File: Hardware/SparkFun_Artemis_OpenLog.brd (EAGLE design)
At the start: 30.5 x 30.5 mm, 140 parts, among them J14 CORTEX_JTAG, J6 MICRO-SD, Q1 20V/0.2A/8MHz/1.2Ω/1Vth, Q10 20V/0.2A/8MHz/1.2Ω/1Vth, Q2 20V/4.2A/52mΩ/1.4W, Q3 20V/0.2A/8MHz/1.2Ω/1Vth, Q7 20V/0.2A/8MHz/1.2Ω/1Vth, Q9 20V/0.2A/8MHz/1.2Ω/1Vth, U1 3.0V Supervisor, U10 CH340E, U13 9DoF IMU, U14 1.8V/100mA, U2 MCP73831, U3 3.3V, U4 3.3V, U8 ARTEMIS_MODULE, Y3 32.768kHz

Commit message: Attempts to update just the Eagle design
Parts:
- removed C51, C52: 0.1uF, SparkFun-Capacitors:0402-TIGHT
- removed C53, C54: 1.0uF, SparkFun-Capacitors:0402-TIGHT
- removed Q1, Q10, Q3, Q7, Q9: 20V/0.2A/8MHz/1.2Ω/1Vth, SparkFun-DiscreteSemi:SOT-416FL
- removed R40, R41, R44, R45, R46, R47, R48: 2.2k, SparkFun-Resistors:0402-TIGHT
- removed R49: DNP, SparkFun-Resistors:0402-TIGHT
- removed U13: 9DoF IMU, SparkFun-Sensors:QFN24-3X3-ICM-20948
- removed U14: 1.8V/100mA, SparkFun-IC-Power:SC70
- added C10, C11, C9: 0.1uF, SparkFun-Capacitors:0402
- added C6, C8: 22pF, SparkFun-Capacitors:0402-TIGHT
- added R10, R11: 4.7k, SparkFun-Resistors:0402-TIGHT
- added R12, R9: 100k, SparkFun-Resistors:0402-TIGHT
- added U5: BNO086, bno086:LGA-28
- added Y1: 32.768kHz, SparkFun-Clocks:CRYSTAL-SMD-3.2X1.5MM
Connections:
- removed net ICM-20948-LV_!CS!: Q9.2, R46.1, U13.22
- removed net ICM-20948-LV_#_1.8V: C52.1, C53.1, Q1.1, Q10.1, Q3.1, Q7.1, Q9.1, R40.2, R41.2, R44.2, R46.2, R48.2, U13.13, U13.8, U14.5
- removed net ICM-20948-LV_INT: Q7.2, R44.1, U13.12
- removed net ICM-20948-LV_SCK: Q1.2, R40.1, U13.23
- removed net ICM-20948-LV_SDI: Q3.2, R41.1, U13.24
- removed net ICM-20948-LV_SDO: Q10.2, R48.1, U13.9
- removed net N$30: C51.1, U13.10
- new net !RST: R9.1, U5.11
- new net N$2: C8.1, U5.27, Y1.P$2
- new net N$3: C6.1, U5.26, Y1.P$1
- new net N$4: C9.1, U5.9
- new net N$5: R12.1, U5.4
- new net S_SCL: R11.1, U5.15
- new net S_SDA: R10.1, U5.16
- net 3.3V: now also C10.1, C11.1, R10.2, R11.2, R12.2, R9.2, U5.28, U5.3, U5.5, U5.6; no longer C54.1, R45.2, R47.2, R49.2, U14.1
- net GND: now also C10.2, C11.2, C6.2, C8.2, C9.2, U5.10, U5.2, U5.25; no longer C51.2, C52.2, C53.2, C54.2, U13.18, U13.20, U14.2
- net ICM_!CS!: now also U5.18; no longer Q9.3, R47.1
- net ICM_INT: now also U5.14; no longer Q7.3, R45.1
- net ICM_PWR: no longer U14.3
- net SCK: now also U5.19; no longer Q1.3
- net SDI: now also U5.20; no longer Q10.3, R49.1
- net SDO: now also U5.17; no longer Q3.3
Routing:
- net ICM-20948-LV_#_1.8V: track 43.4 -> 0.00 mm, vias 4 -> 0
- net ICM_PWR: track 41.5 -> 0.00 mm, vias 3 -> 0
- net ICM_!CS!: track 34.6 -> 15.5 mm, vias 3 -> 2
- net SCK: track 53.8 -> 70.2 mm, vias 3 -> 4
- net S_SDA: track 0.00 -> 7.80 mm
- net SDO: track 32.7 -> 27.1 mm
- net ICM-20948-LV_!CS!: track 5.56 -> 0.00 mm
- net GND: track 17.3 -> 11.8 mm, vias 35 -> 30
- net S_SCL: track 0.00 -> 5.34 mm
- net ICM-20948-LV_SDO: track 5.13 -> 0.00 mm
- net N$3: track 0.00 -> 4.81 mm
- net ICM-20948-LV_SCK: track 4.65 -> 0.00 mm
- net N$2: track 0.00 -> 4.35 mm
- net 3.3V: track 32.1 -> 36.3 mm, vias 9 -> 10
- net ICM-20948-LV_SDI: track 4.14 -> 0.00 mm
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
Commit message: Moves some parts around
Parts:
- moved R9 10.8 mm to (25.4, 9.91), flipped to the bottom, turned to 180 degrees
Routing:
- net SCK: track 70.2 -> 24.1 mm, vias 4 -> 2
- net ICM_INT: track 15.5 -> 9.84 mm
- net ICM_!CS!: track 15.5 -> 20.6 mm
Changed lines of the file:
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@@
 <attribute name="VALUE" x="27.686" y="13.462" size="0.6096" layer="28" font="vector" ratio="20" rot="MR0" align="top-center"/>
 </element>
-<element name="R9" library="SparkFun-Resistors" package="0402-TIGHT" value="100k" x="32.258" y="18.288" smashed="yes">
-<attribute name="NAME" x="32.258" y="18.85" size="0.6096" layer="25" font="vector" ratio="20" align="bottom-center"/>
-<attribute name="PROD_ID" value="RES-13495" x="33.528" y="18.288" size="1.778" layer="27" display="off"/>
-<attribute name="VALUE" x="32.258" y="17.726" size="0.6096" layer="27" font="vector" ratio="20" align="top-center"/>
+<element name="R9" library="SparkFun-Resistors" package="0402-TIGHT" value="100k" x="25.4" y="9.906" smashed="yes" rot="MR180">
+<attribute name="NAME" x="25.4" y="9.344" size="0.6096" layer="26" font="vector" ratio="20" rot="MR180" align="bottom-center"/>
+<attribute name="PROD_ID" value="RES-13495" x="26.67" y="9.906" size="1.778" layer="28" rot="MR180" display="off"/>
+<attribute name="VALUE" x="25.4" y="10.468" size="0.6096" layer="28" font="vector" ratio="20" rot="MR180" align="top-center"/>
 </element>
 </elements>
@@
 <wire x1="28.42" y1="19.022" x2="27.94" y2="18.542" width="0.1524" layer="16"/>
 <wire x1="27.94" y1="18.542" x2="27.94" y2="18.034" width="0.1524" layer="16"/>
-<wire x1="18.07" y1="2.04" x2="32.758" y2="18.288" width="0" layer="19" extent="1-16"/>
+<wire x1="25.9" y1="10.922" x2="25.9" y2="9.906" width="0" layer="19" extent="16-16"/>
 </signal>
 <signal name="VIN" class="1">
@@
 <wire x1="12.462" y1="24.4" x2="11.54" y2="24.4" width="0.1524" layer="1"/>
 <wire x1="12.922" y1="23.273" x2="12.795" y2="23.4" width="0.1524" layer="16"/>
-<wire x1="17.1096" y1="1.1784" x2="17.1096" y2="1.63634375" width="0.1524" layer="16"/>
-<wire x1="14.3002" y1="4.44574375" x2="14.3002" y2="6.7175125" width="0.1524" layer="16"/>
-<wire x1="17.1096" y1="1.1784" x2="17.3806" y2="0.9074" width="0.1524" layer="16"/>
-<wire x1="17.1096" y1="1.63634375" x2="14.3002" y2="4.44574375" width="0.1524" layer="16"/>
-<via x="13.081" y="8.2804" extent="1-16" drill="0.3048"/>
-<wire x1="13.081" y1="8.2804" x2="13.081" y2="7.9367125" width="0.1524" layer="16"/>
-<wire x1="13.081" y1="7.9367125" x2="14.3002" y2="6.7175125" width="0.1524" layer="16"/>
-<wire x1="12.827" y1="12.827" x2="12.827" y2="8.5344" width="0.1524" layer="1"/>
-<wire x1="13.081" y1="8.2804" x2="12.827" y2="8.5344" width="0.1524" layer="1"/>
-<wire x1="12.3698" y1="13.2842" x2="10.92274375" y2="13.2842" width="0.1524" layer="1"/>
-<wire x1="10.92274375" y1="13.2842" x2="10.033" y2="14.17394375" width="0.1524" layer="1"/>
-<wire x1="12.827" y1="12.827" x2="12.3698" y2="13.2842" width="0.1524" layer="1"/>
-<wire x1="10.033" y1="14.859" x2="10.033" y2="14.17394375" width="0.1524" layer="1"/>
-<via x="10.033" y="14.859" extent="1-16" drill="0.3048"/>
 <contactref element="J6" pad="SCLK"/>
-<wire x1="13.462" y1="21.4224" x2="12.922" y2="21.9624" width="0.1524" layer="16"/>
-<wire x1="15.553671875" y1="21.014671875" x2="15.14594375" y2="21.4224" width="0.1524" layer="16"/>
-<wire x1="15.14594375" y1="21.4224" x2="13.462" y2="21.4224" width="0.1524" layer="16"/>
-<wire x1="12.922" y1="21.9624" x2="12.922" y2="23.273" width="0.1524" layer="16"/>
-<wire x1="10.033" y1="14.859" x2="10.033" y2="16.91905625" width="0.1524" layer="16"/>
-<wire x1="12.79894375" y1="19.685" x2="15.113" y2="19.685" width="0.1524" layer="16"/>
-<wire x1="15.113" y1="19.685" x2="15.553671875" y2="20.125671875" width="0.1524" layer="16"/>
-<wire x1="15.553671875" y1="20.125671875" x2="15.553671875" y2="21.014671875" width="0.1524" layer="16"/>
-<wire x1="10.033" y1="16.91905625" x2="12.79894375" y2="19.685" width="0.1524" layer="16"/>
-<wire x1="23.2594" y1="0.9074" x2="23.622" y2="1.27" width="0.1524" layer="16"/>
-<wire x1="24.638" y1="3.5237125" x2="25.4" y2="4.2857125" width="0.1524" layer="16"/>
-<wire x1="17.3806" y1="0.9074" x2="23.2594" y2="0.9074" width="0.1524" layer="16"/>
-<wire x1="23.622" y1="1.27" x2="23.622" y2="1.85494375" width="0.1524" layer="16"/>
-<wire x1="23.622" y1="1.85494375" x2="24.638" y2="2.87094375" width="0.1524" layer="16"/>
-<wire x1="24.638" y1="2.87094375" x2="24.638" y2="3.5237125" width="0.1524" layer="16"/>
-<wire x1="25.4" y1="4.2857125" x2="25.4" y2="8.255" width="0.1524" layer="16"/>
 <contactref element="U5" pad="19"/>
 <wire x1="12.7" y1="24.638" x2="12.7" y2="28.194" width="0.1524" layer="2"/>
@@
 <wire x1="22.65794375" y1="28.3376" x2="21.0654" y2="28.3376" width="0.1524" layer="1"/>
 <wire x1="21.0654" y1="28.3376" x2="20.503" y2="28.9" width="0.1524" layer="1"/>
-<wire x1="26.027" y1="25.1968" x2="26.28025625" y2="25.1968" width="0.1524" layer="16"/>
-<wire x1="26.78825625" y1="24.6888" x2="28.86754375" y2="24.6888" width="0.1524" layer="16"/>
-<wire x1="28.86754375" y1="24.6888" x2="29.03274375" y2="24.5236" width="0.1524" layer="16"/>
-<wire x1="29.8656" y1="24.3896875" x2="29.8656" y2="23.1346" width="0.1524" layer="16"/>
 <wire x1="24.5538" y1="26.67" x2="26.027" y2="25.1968" width="0.1524" layer="16"/>
-<wire x1="26.28025625" y1="25.1968" x2="26.78825625" y2="24.6888" width="0.1524" layer="16"/>
-<wire x1="29.03274375" y1="24.5236" x2="29.7316875" y2="24.5236" width="0.1524" layer="16"/>
-<wire x1="29.7316875" y1="24.5236" x2="29.8656" y2="24.3896875" width="0.1524" layer="16"/>
-<wire x1="29.8656" y1="23.1346" x2="29.726" y2="22.995" width="0.1524" layer="16"/>
 <contactref element="U5" pad="14"/>
-<wire x1="24.92" y1="16.08" x2="29.726" y2="22.995" width="0" layer="19" extent="16-16"/>
+<wire x1="24.92" y1="16.08" x2="26.027" y2="25.1968" width="0" layer="19" extent="16-16"/>
 </signal>
 <signal name="ICM_!CS!">
 <contactref element="U8" pad="~D44"/>
-<wire x1="29.7616" y1="24.5054" x2="29.591" y2="24.676" width="0.1524" layer="1"/>
-<wire x1="29.591" y1="24.676" x2="29.591" y2="25.057" width="0.1524" layer="1"/>
 <via x="23.368" y="29.591" extent="1-16" drill="0.3048"/>
 <wire x1="23.51274375" y1="29.73574375" x2="23.368" y2="29.591" width="0.1524" layer="16"/>
@@
 <wire x1="21.2046" y1="28.6424" x2="20.447" y2="29.4" width="0.1524" layer="1"/>
 <wire x1="22.5316875" y1="28.6424" x2="21.2046" y2="28.6424" width="0.1524" layer="1"/>
-<via x="29.591" y="25.057" extent="1-16" drill="0.3048"/>
-<wire x1="26.1874" y1="25.5016" x2="26.4065125" y2="25.5016" width="0.1524" layer="16"/>
 <wire x1="24.9856" y1="29.22043125" x2="24.9856" y2="26.7034" width="0.1524" layer="16"/>
 <wire x1="24.9856" y1="26.7034" x2="26.1874" y2="25.5016" width="0.1524" layer="16"/>
-<wire x1="26.4065125" y1="25.5016" x2="26.8511125" y2="25.057" width="0.1524" layer="16"/>
-<wire x1="26.8511125" y1="25.057" x2="29.591" y2="25.057" width="0.1524" layer="16"/>
 <contactref element="U5" pad="18"/>
-<wire x1="24.27" y1="18.03" x2="29.7616" y2="24.5054" width="0" layer="19" extent="1-16"/>
+<wire x1="24.27" y1="18.03" x2="24.274" y2="18.034" width="0.1524" layer="16"/>
+<wire x1="24.274" y1="18.034" x2="25.654" y2="18.034" width="0.1524" layer="16"/>
+<via x="25.654" y="18.034" extent="1-16" drill="0.35"/>
+<wire x1="25.654" y1="18.034" x2="25.654" y2="23.84555625" width="0.1524" layer="2"/>
+<wire x1="25.654" y1="23.84555625" x2="25.5905" y2="23.90905625" width="0.1524" layer="2"/>
+<wire x1="25.5905" y1="23.90905625" x2="25.5905" y2="25.0825" width="0.1524" layer="2"/>
+<wire x1="25.5905" y1="25.0825" x2="26.162" y2="25.654" width="0.1524" layer="2"/>
+<wire x1="26.162" y1="25.654" x2="26.1874" y2="25.5016" width="0" layer="19" extent="2-16"/>
 </signal>
 <signal name="VREG_EN">
@@
 <contactref element="U5" pad="11"/>
 <contactref element="R9" pad="1"/>
-<wire x1="31.758" y1="18.288" x2="26.42" y2="16.08" width="0" layer="19" extent="1-16"/>
+<wire x1="24.9" y1="9.906" x2="26.42" y2="16.08" width="0" layer="19" extent="16-16"/>
 </signal>
 <signal name="N$2">

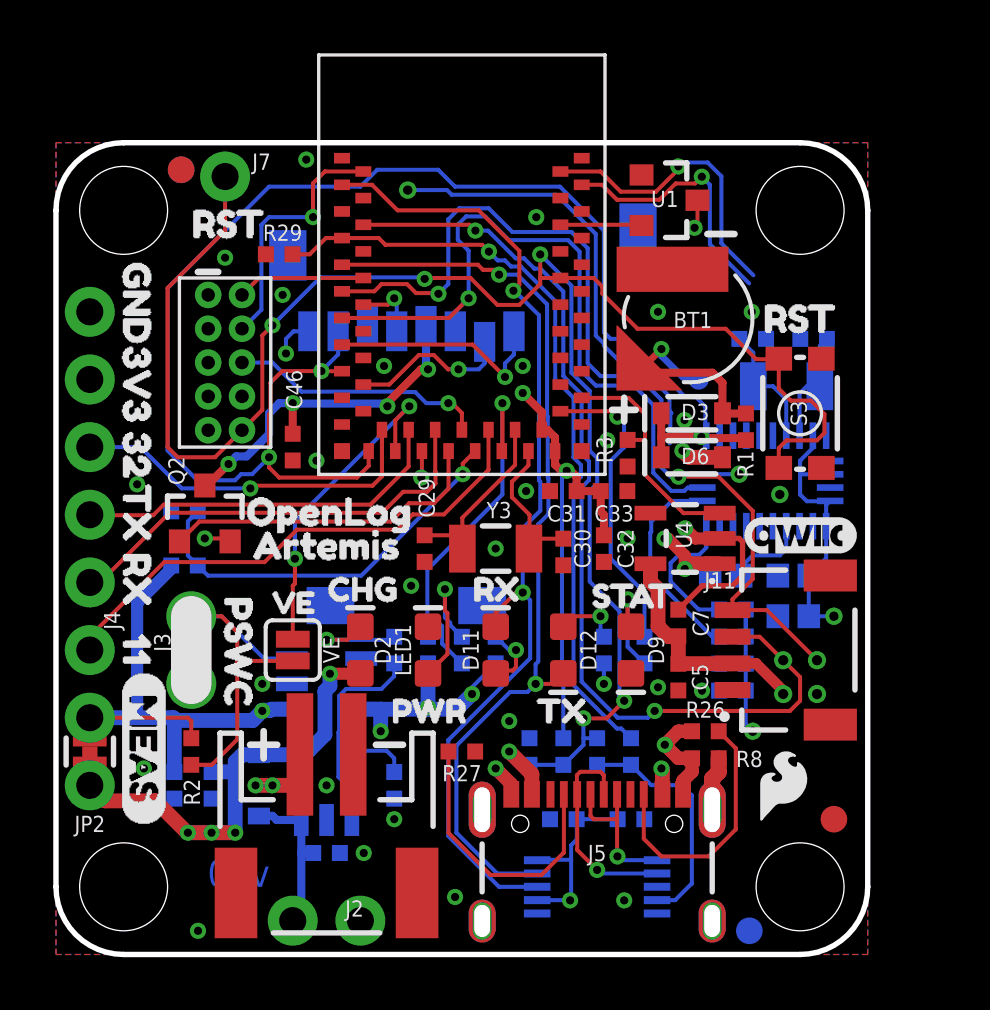
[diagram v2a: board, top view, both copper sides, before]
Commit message: Routes all nets - DRC is clean
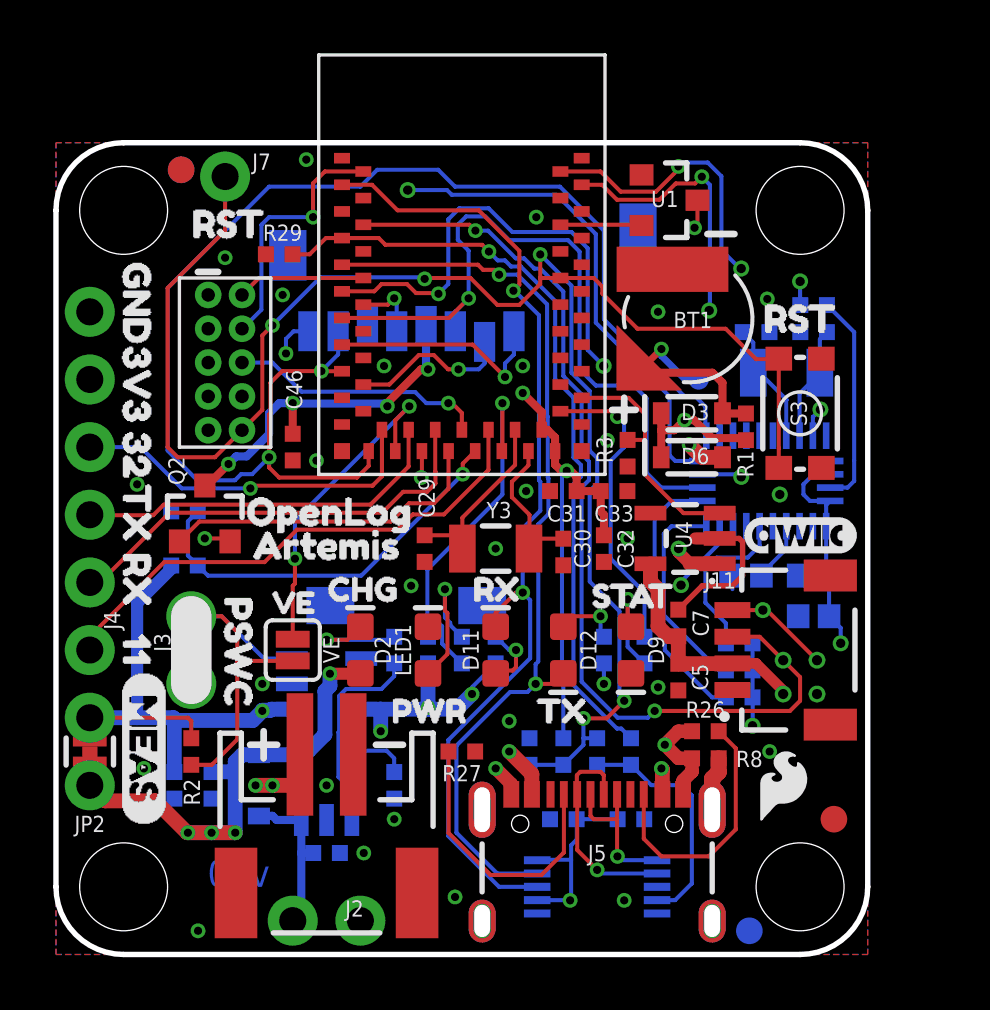
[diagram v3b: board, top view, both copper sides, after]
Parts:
- moved R12 13.8 mm to (28.4, 24.4), turned to 0 degrees
- moved R10 2.30 mm to (25.7, 9.65)
- moved R11 2.30 mm to (25.7, 10.7)
- moved R9 1.80 mm to (25.7, 11.7)
- moved C10 0.76 mm to (28.4, 12.7)
- moved C11 0.76 mm to (28.4, 14.2)
- moved C9 0.76 mm to (25.9, 14.2)
- moved Y1 0.51 mm to (27.4, 21.8)
- moved C6 0.28 mm to (26.3, 23.4)
- moved C8 0.25 mm to (28.4, 23.4)
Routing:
- net ICM_INT: track 9.84 -> 24.1 mm, vias 1 -> 3
- net N$5: track 0.00 -> 8.04 mm
- net !RST: track 0.00 -> 6.24 mm
- net 3.3V: track 36.3 -> 33.4 mm, vias 10 -> 12
- net S_SCL: track 5.34 -> 7.95 mm
- net ARTEMIS_!RESET: track 72.5 -> 70.0 mm
- net S_SDA: track 7.80 -> 10.2 mm
- net SCK: track 24.1 -> 25.5 mm
- net VIN: track 24.3 -> 23.2 mm, vias 3 -> 2
- net N$4: track 3.15 -> 2.24 mm
- net ICM_!CS!: track 20.6 -> 20.2 mm, vias 2 -> 3
- net SCL: track 35.2 -> 35.5 mm, vias 2 -> 3
- net VCC_1: track 33.0 -> 32.7 mm, vias 4 -> 3
- net GND: vias 30 -> 29
